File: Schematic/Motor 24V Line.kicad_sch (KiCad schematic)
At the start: 41 parts, among them J11 5V_SYNC_MODES, Q31 CSD19531Q5A, Q32 CSD19531Q5A, U15 LM25190RGYR

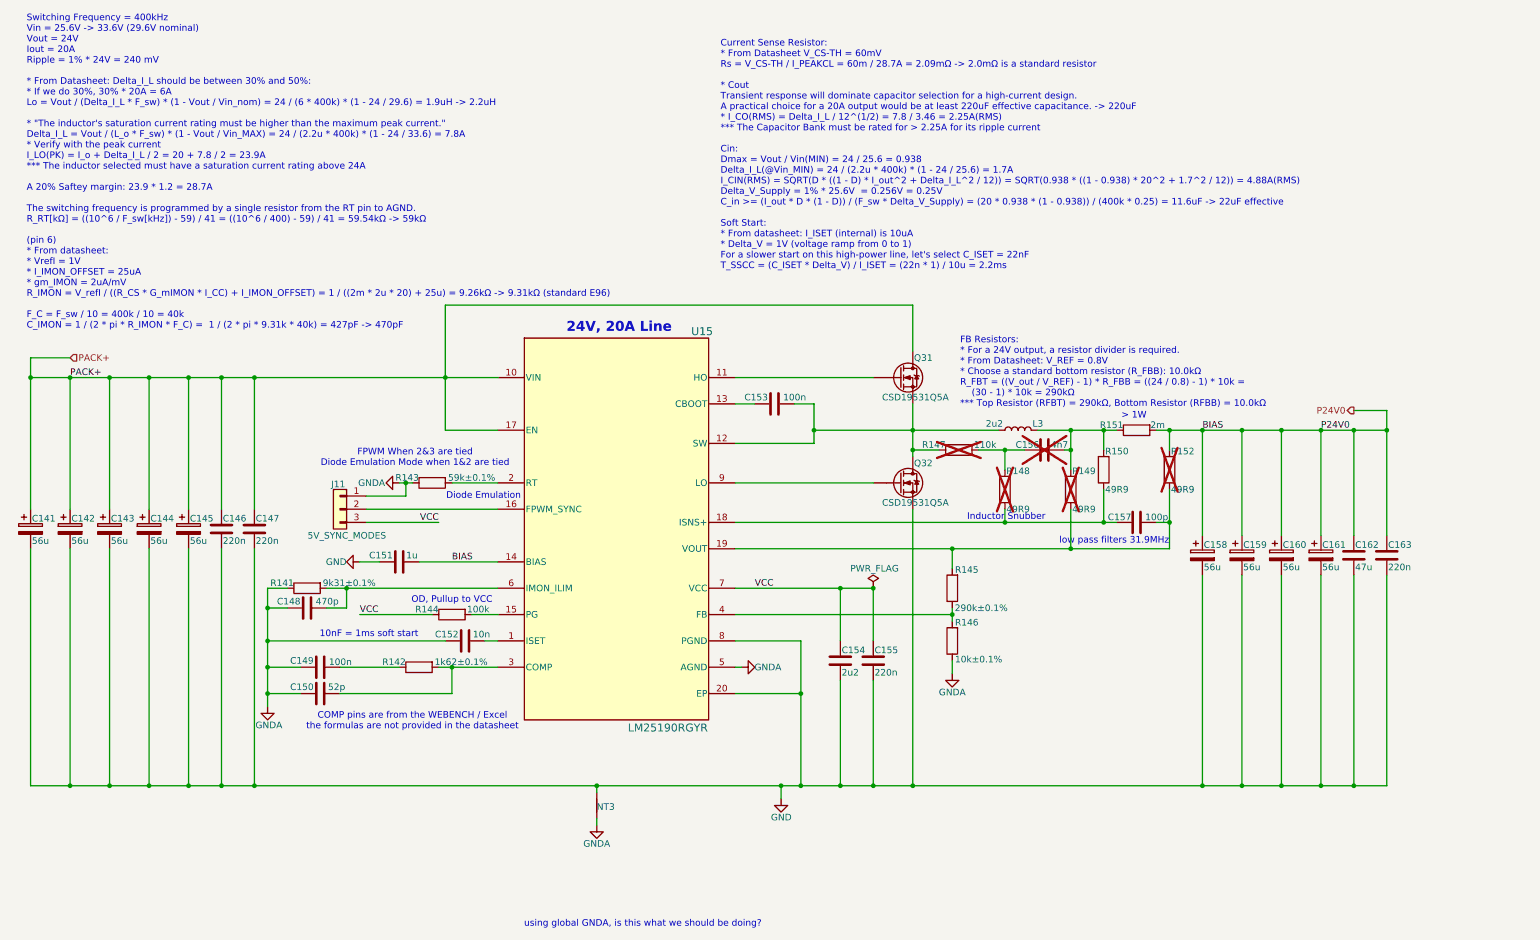
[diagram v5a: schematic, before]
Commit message: Added MCU
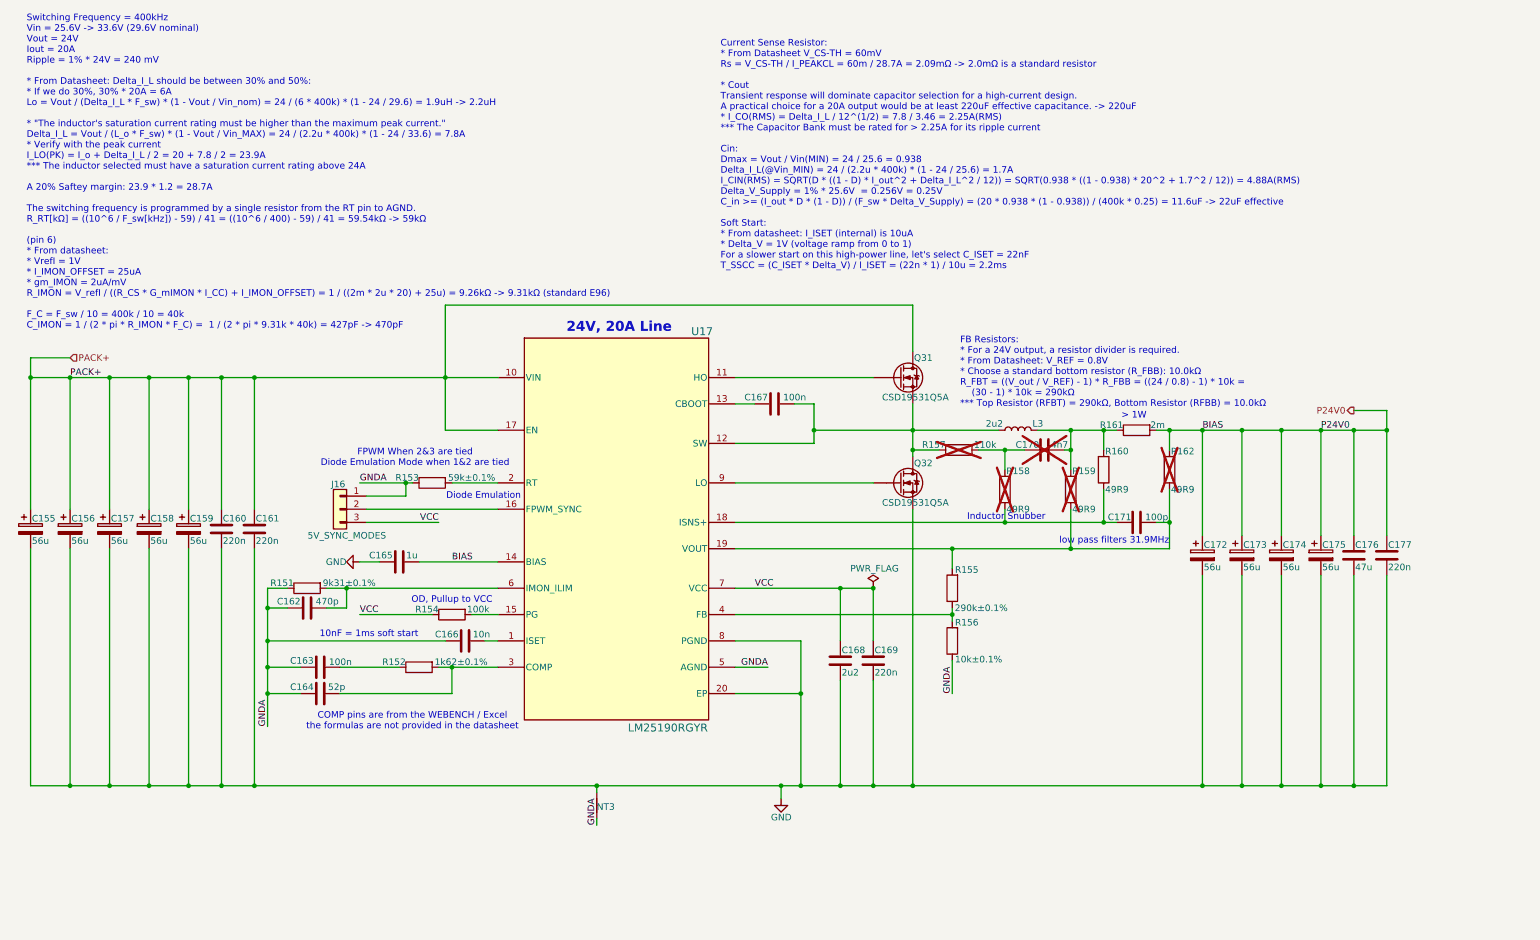
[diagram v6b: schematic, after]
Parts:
- renumbered C141 to C155, C142 to C156, C143 to C157, C144 to C158, C145 to C159, C146 to C160, C147 to C161, C148 to C162, C149 to C163, C150 to C164, C151 to C165, C152 to C166, C153 to C167, C154 to C168, C155 to C169, C156 to C170, C157 to C171, C158 to C172, C159 to C173, C160 to C174, C161 to C175, C162 to C176, C163 to C177, J11 to J16, R141 to R151, R142 to R152, R143 to R153, R144 to R154, R145 to R155, R146 to R156, R147 to R157, R148 to R158, R149 to R159, R150 to R160, R151 to R161, R152 to R162, U15 to U17
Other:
- note removed: "using global GNDA, is this what we should be doing?"

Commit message: Started to work on the BOM
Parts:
- removed C176: 47u, symbol Device:C
- added C175: 56u, AHA0810560M040R:CAPAE830X1100M, symbol Device:C_Polarized
- C154: renamed from C155; footprint (none) -> AHA0810560M040R:CAPAE830X1100M; Link (none) -> https://mou.sr/4g6lc2W; Manufacturer Part Number (none) -> AHA0810560M040R; Price per Unit (none) -> 1.50; Supplier (none) -> Mouser; Supplier Part Number (none) -> 581-AHA0810560M040R
- C155: renamed from C156; footprint (none) -> AHA0810560M040R:CAPAE830X1100M; Link (none) -> https://mou.sr/4g6lc2W; Manufacturer Part Number (none) -> AHA0810560M040R; Price per Unit (none) -> 1.50; Supplier (none) -> Mouser; Supplier Part Number (none) -> 581-AHA0810560M040R
- C156: renamed from C157; footprint (none) -> AHA0810560M040R:CAPAE830X1100M; Link (none) -> https://mou.sr/4g6lc2W; Manufacturer Part Number (none) -> AHA0810560M040R; Price per Unit (none) -> 1.50; Supplier (none) -> Mouser; Supplier Part Number (none) -> 581-AHA0810560M040R
- C157: renamed from C158; footprint (none) -> AHA0810560M040R:CAPAE830X1100M; Link (none) -> https://mou.sr/4g6lc2W; Manufacturer Part Number (none) -> AHA0810560M040R; Price per Unit (none) -> 1.50; Supplier (none) -> Mouser; Supplier Part Number (none) -> 581-AHA0810560M040R
- C158: renamed from C159; footprint (none) -> AHA0810560M040R:CAPAE830X1100M; Link (none) -> https://mou.sr/4g6lc2W; Manufacturer Part Number (none) -> AHA0810560M040R; Price per Unit (none) -> 1.50; Supplier (none) -> Mouser; Supplier Part Number (none) -> 581-AHA0810560M040R
- C159: renamed from C160; footprint (none) -> Capacitor_SMD:C_0805_2012Metric_Pad1.18x1.45mm_HandSolder; Link (none) -> https://mou.sr/42gipOV; Manufacturer Part Number (none) -> CL21B224KBFNFNE; Price per Unit (none) -> 0.10; Supplier (none) -> Mouser; Supplier Part Number (none) -> 187-CL21B224KBFNFNE
- C160: renamed from C161; footprint (none) -> Capacitor_SMD:C_0805_2012Metric_Pad1.18x1.45mm_HandSolder; Link (none) -> https://mou.sr/42gipOV; Manufacturer Part Number (none) -> CL21B224KBFNFNE; Price per Unit (none) -> 0.10; Supplier (none) -> Mouser; Supplier Part Number (none) -> 187-CL21B224KBFNFNE
- C161: renamed from C162; footprint (none) -> Capacitor_SMD:C_0603_1608Metric_Pad1.08x0.95mm_HandSolder; Link (none) -> https://mou.sr/3UXYSz1; Manufacturer Part Number (none) -> CL10C471JB8NNND; Price per Unit (none) -> 0.10; Supplier (none) -> Mouser; Supplier Part Number (none) -> 187-CL10C471JB8NNND
- C162: renamed from C163; footprint (none) -> Capacitor_SMD:C_1206_3216Metric_Pad1.33x1.80mm_HandSolder; Link (none) -> https://mou.sr/4n9ybmQ; Manufacturer Part Number (none) -> CL31B104KBCNNNC; Price per Unit (none) -> 0.11; Supplier (none) -> Mouser; Supplier Part Number (none) -> 187-CL31B104KBCNNNC
- C163: renamed from C164; value 52p -> 62p; footprint (none) -> Capacitor_SMD:C_0603_1608Metric_Pad1.08x0.95mm_HandSolder; Link (none) -> https://mou.sr/3JK05aN; Manufacturer Part Number (none) -> GCM1885C2A620FA16D; Price per Unit (none) -> 0.14; Supplier (none) -> Mouser; Supplier Part Number (none) -> 81-GCM1885C2A620FA6D
- C164: renamed from C165; footprint (none) -> Capacitor_SMD:C_1206_3216Metric_Pad1.33x1.80mm_HandSolder; Link (none) -> https://mou.sr/41y0aEA; Manufacturer Part Number (none) -> CL31B105KBHNNNE; Price per Unit (none) -> 0.11; Supplier (none) -> Mouser; Supplier Part Number (none) -> 187-CL31B105KBHNNNE
- C165: renamed from C166; footprint (none) -> Capacitor_SMD:C_1206_3216Metric_Pad1.33x1.80mm_HandSolder; Link (none) -> https://mou.sr/3OC0xXF; Manufacturer Part Number (none) -> CL31B103KHFNFNE; Price per Unit (none) -> 0.13; Supplier (none) -> Mouser; Supplier Part Number (none) -> 187-CL31B103KHFNFNE
- C166: renamed from C167; footprint (none) -> Capacitor_SMD:C_1206_3216Metric_Pad1.33x1.80mm_HandSolder; Link (none) -> https://mou.sr/4n9ybmQ; Manufacturer Part Number (none) -> CL31B104KBCNNNC; Price per Unit (none) -> 0.11; Supplier (none) -> Mouser; Supplier Part Number (none) -> 187-CL31B104KBCNNNC
- C167: renamed from C168; footprint (none) -> Capacitor_SMD:C_1206_3216Metric_Pad1.33x1.80mm_HandSolder; Link (none) -> https://mou.sr/3VA1gvS; Manufacturer Part Number (none) -> CL31A225KB9LNNC; Price per Unit (none) -> 0.15; Supplier (none) -> Mouser; Supplier Part Number (none) -> 187-CL31A225KB9LNNC
- C168: renamed from C169; footprint (none) -> Capacitor_SMD:C_0805_2012Metric_Pad1.18x1.45mm_HandSolder; Link (none) -> https://mou.sr/42gipOV; Manufacturer Part Number (none) -> CL21B224KBFNFNE; Price per Unit (none) -> 0.10; Supplier (none) -> Mouser; Supplier Part Number (none) -> 187-CL21B224KBFNFNE
- C169: renamed from C170; footprint (none) -> Capacitor_SMD:C_0603_1608Metric_Pad1.08x0.95mm_HandSolder; Link (none) -> https://mou.sr/4g6fuOy; Manufacturer Part Number (none) -> CL10B472KB8NFNC; Price per Unit (none) -> 0.10; Supplier (none) -> Mouser; Supplier Part Number (none) -> 187-CL10B472KB8NFNC
- C170: renamed from C171; footprint (none) -> Capacitor_SMD:C_0603_1608Metric_Pad1.08x0.95mm_HandSolder; Link (none) -> https://mou.sr/4kcxpDX; Manufacturer Part Number (none) -> CL10C101JB8NNNC; Price per Unit (none) -> 0.10; Supplier (none) -> Mouser; Supplier Part Number (none) -> 187-CL10C101JB8NNNC
- C171: renamed from C172; footprint (none) -> AHA0810560M040R:CAPAE830X1100M; Link (none) -> https://mou.sr/4g6lc2W; Manufacturer Part Number (none) -> AHA0810560M040R; Price per Unit (none) -> 1.50; Supplier (none) -> Mouser; Supplier Part Number (none) -> 581-AHA0810560M040R
- C172: renamed from C173; footprint (none) -> AHA0810560M040R:CAPAE830X1100M; Link (none) -> https://mou.sr/4g6lc2W; Manufacturer Part Number (none) -> AHA0810560M040R; Price per Unit (none) -> 1.50; Supplier (none) -> Mouser; Supplier Part Number (none) -> 581-AHA0810560M040R
- C173: renamed from C174; footprint (none) -> AHA0810560M040R:CAPAE830X1100M; Link (none) -> https://mou.sr/4g6lc2W; Manufacturer Part Number (none) -> AHA0810560M040R; Price per Unit (none) -> 1.50; Supplier (none) -> Mouser; Supplier Part Number (none) -> 581-AHA0810560M040R
- C174: renamed from C175; footprint (none) -> AHA0810560M040R:CAPAE830X1100M; Link (none) -> https://mou.sr/4g6lc2W; Manufacturer Part Number (none) -> AHA0810560M040R; Price per Unit (none) -> 1.50; Supplier (none) -> Mouser; Supplier Part Number (none) -> 581-AHA0810560M040R
- C176: renamed from C177; footprint (none) -> Capacitor_SMD:C_0805_2012Metric_Pad1.18x1.45mm_HandSolder; Link (none) -> https://mou.sr/42gipOV; Manufacturer Part Number (none) -> CL21B224KBFNFNE; Price per Unit (none) -> 0.10; Supplier (none) -> Mouser; Supplier Part Number (none) -> 187-CL21B224KBFNFNE
- L3: footprint (none) -> Capacitor_SMD:C_1206_3216Metric_Pad1.33x1.80mm_HandSolder; Link (none) -> https://mou.sr/3VA1gvS; Manufacturer Part Number (none) -> CL31A225KB9LNNC; Price per Unit (none) -> 0.15; Supplier (none) -> Mouser; Supplier Part Number (none) -> 187-CL31A225KB9LNNC
- Q31, Q32: footprint Package_TO_SOT_SMD:TDSON-8-1 -> (none)
- U15: renamed from U17; footprint RGY0019C-MFG -> (none)
- renumbered J16 to J14, R151 to R147, R152 to R148, R153 to R149, R154 to R150, R155 to R151, R156 to R152, R157 to R153, R158 to R154, R159 to R155, R160 to R156, R161 to R157, R162 to R158
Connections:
- net GND: now also C175.2
- net P24V0: now also C175.1
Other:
- moved on the sheet: C176

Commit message: Massive pivit, simplification
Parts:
- renumbered C154 to C147, C155 to C148, C156 to C149, C157 to C150, C158 to C151, C159 to C152, C160 to C153, C161 to C154, C162 to C155, C163 to C156, C164 to C157, C165 to C158, C166 to C159, C167 to C160, C168 to C161, C169 to C162, C170 to C163, C171 to C164, C172 to C165, C173 to C166, C174 to C167, C175 to C168, C176 to C169, J14 to J12, U15 to U14
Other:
- note added: "Current Sense Resistor: * From Datasheet V_CS-TH = 60mV Rs = V_CS-TH / I_PEAKCL = 60m / 28.7A = 2.09mΩ -> 2.0mΩ is a standard resistor * Cout Cout = Delta_IL / (8 * F_sw * Delta_Vout) = 7.8 / (8 * 400k * 0.240) = 10.2uF Cout >= (Lo * (Delta_ILoad)^2) / ((Vout + Delta_Vovershoot)^2 - Vout^2) >= (2.2u* 10^2) / ((24 + 0.72)^2 - 24^2) >= 6.3uF * I_CO(RMS) = Delta_I_L / 12^(1/2) = 7.8 / 3.46 = 2.25A(R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"
- note removed: "Current Sense Resistor: * From Datasheet V_CS-TH = 60mV Rs = V_CS-TH / I_PEAKCL = 60m / 28.7A = 2.09mΩ -> 2.0mΩ is a standard resistor * Cout Transient response will dominate capacitor selection for a high-current design. A practical choice for a 20A output would be at least 220uF effective capacitance. -> 220uF * I_CO(RMS) = Delta_I_L / 12^(1/2) = 7.8 / 3.46 = 2.25A(RMS) *** The Capacitor Bank m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"
